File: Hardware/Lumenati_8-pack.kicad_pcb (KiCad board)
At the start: 2 copper layers, 28.4 x 28.4 mm, 38 parts, among them J1 M01PTH, J2 M01PTH, J3 M01PTH, J4 M01PTH, J5 M01PTH, J6 M01PTH, J7 M01PTH, J8 M01PTH, U1 APA102, U2 APA102, U3 APA102, U4 APA102, U5 APA102, U6 APA102, U7 APA102, U8 APA102

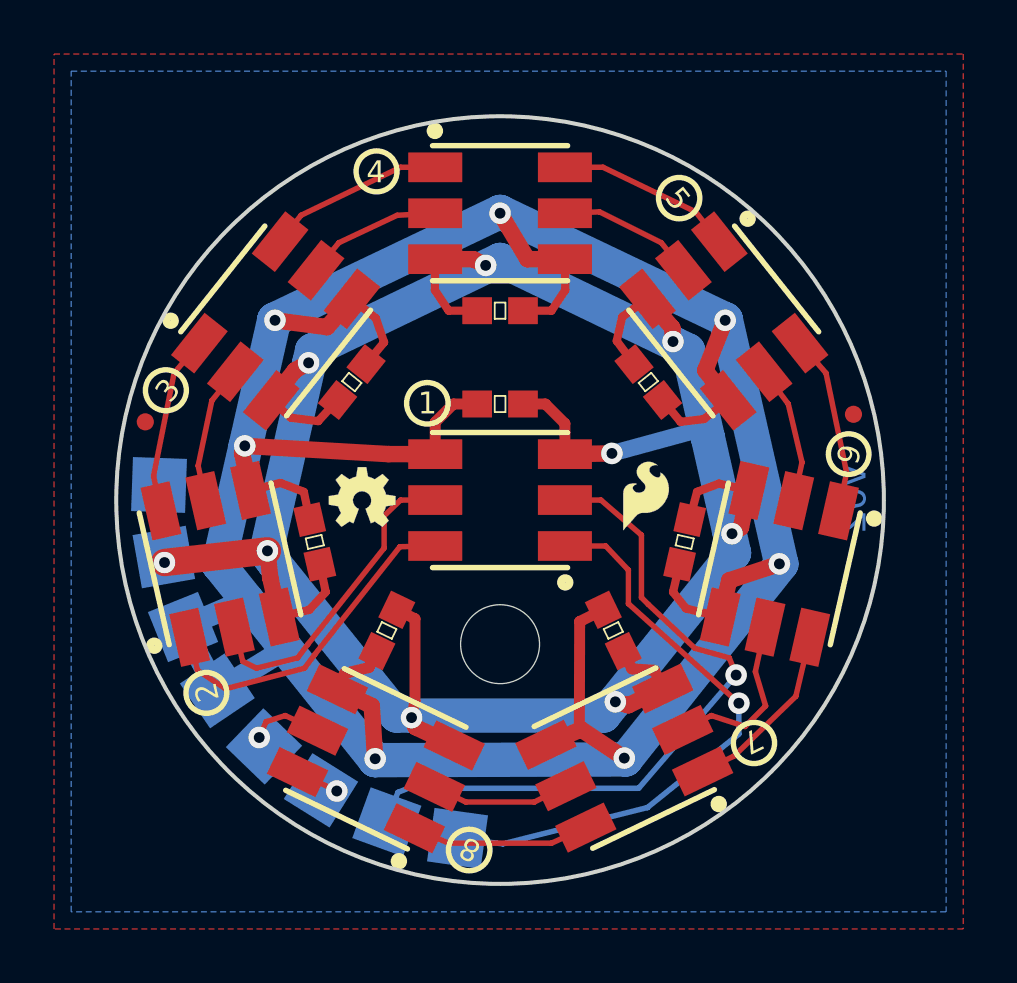
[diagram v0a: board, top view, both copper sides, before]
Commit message: Changed all the names to Lumenati, updated version to v10.
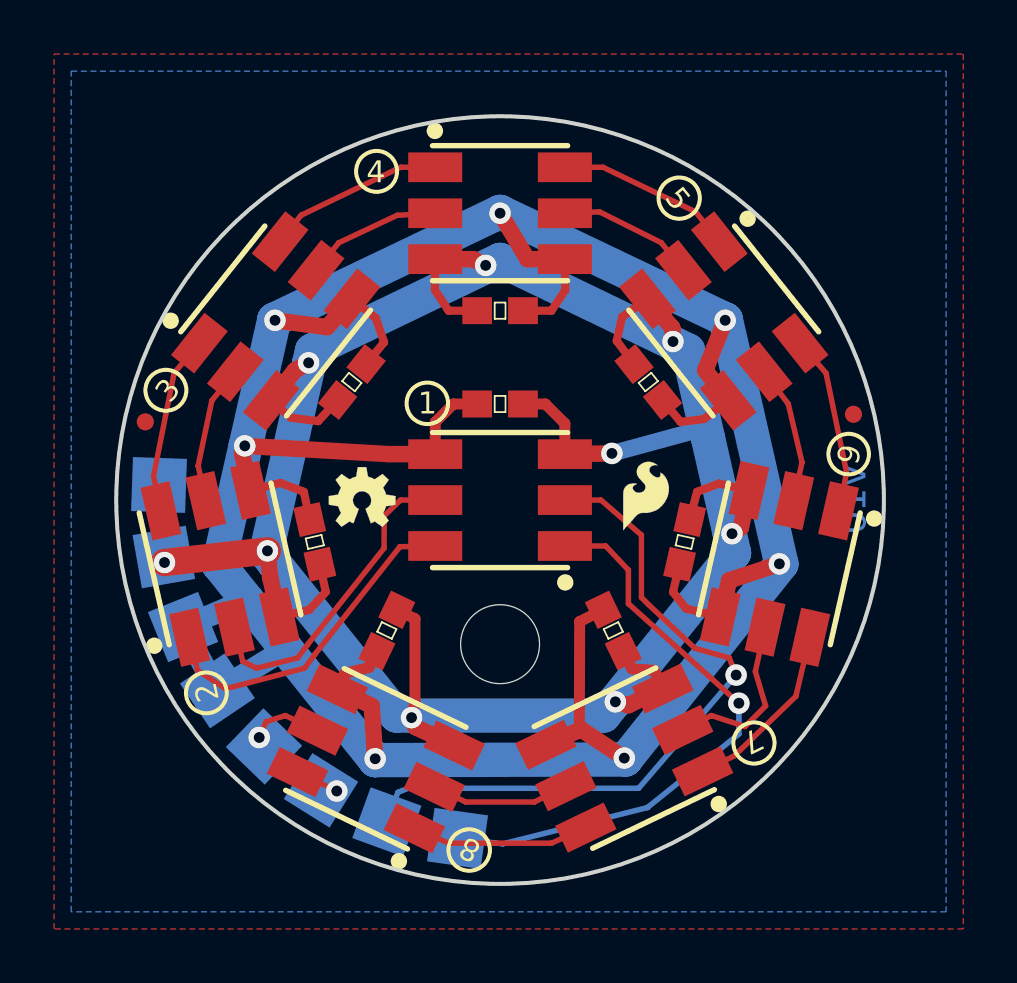
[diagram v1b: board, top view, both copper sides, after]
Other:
- board text added: "Lumenati 8-pack"
- board text added: "v10"
- board text removed: "HiBeam 8-pack"
- board text removed: "HiBeams 8-pack"
- board text removed: "v02"
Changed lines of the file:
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@@
     (35 F.Paste user hide)
     (36 B.SilkS user)
-    (37 F.SilkS user hide)
+    (37 F.SilkS user)
     (38 B.Mask user hide)
     (39 F.Mask user)
-    (40 Dwgs.User user hide)
-    (41 Cmts.User user hide)
+    (40 Dwgs.User user)
+    (41 Cmts.User user)
     (42 Eco1.User user hide)
     (43 Eco2.User user hide)
@@
     (pad_to_mask_clearance 0.1016)
     (aux_axis_origin 0 0)
-    (visible_elements FFF97F7F)
+    (visible_elements FFF9FF7F)
     (pcbplotparams
       (layerselection 0x010fc_ffffffff)
@@
       (net 2 GND))
   )
-  (gr_circle (center 145.542 110.744) (end 146.177 111.1758) (layer F.SilkS) (width 0.2))
-  (gr_circle (center 142.113 85.6234) (end 142.6972 86.106) (layer F.SilkS) (width 0.2))
-  (gr_circle (center 153.3144 86.614) (end 154.0256 86.8934) (layer F.SilkS) (width 0.2))
-  (gr_circle (center 156.083 106.7816) (end 156.7434 107.1626) (layer F.SilkS) (width 0.2))
-  (gr_circle (center 159.5882 96.0882) (end 160.274 96.393) (layer F.SilkS) (width 0.2))
-  (gr_circle (center 135.8138 104.9274) (end 136.3218 105.4862) (layer F.SilkS) (width 0.2))
-  (gr_circle (center 143.9926 94.2086) (end 144.6276 94.6404) (layer F.SilkS) (width 0.2))
-  (gr_circle (center 134.3152 93.726) (end 134.8994 94.2086) (layer F.SilkS) (width 0.2))
+  (gr_circle (center 145.542 110.744) (end 146.177 111.1758) (layer F.SilkS) (width 0.15))
+  (gr_circle (center 142.113 85.6234) (end 142.6972 86.106) (layer F.SilkS) (width 0.15))
+  (gr_circle (center 153.3144 86.614) (end 154.0256 86.8934) (layer F.SilkS) (width 0.15))
+  (gr_circle (center 156.083 106.7816) (end 156.7434 107.1626) (layer F.SilkS) (width 0.15))
+  (gr_circle (center 159.5882 96.0882) (end 160.274 96.393) (layer F.SilkS) (width 0.15))
+  (gr_circle (center 135.8138 104.9274) (end 136.3218 105.4862) (layer F.SilkS) (width 0.15))
+  (gr_circle (center 143.9926 94.2086) (end 144.6276 94.6404) (layer F.SilkS) (width 0.15))
+  (gr_circle (center 134.3152 93.726) (end 134.8994 94.2086) (layer F.SilkS) (width 0.15))
   (gr_text 8 (at 145.5674 110.7186 154.3) (layer F.SilkS)
     (effects (font (size 0.8128 0.8128) (thickness 0.1778)))
@@
     (arrow2b (pts (xy 160.909 128.1938) (xy 159.782496 128.780221)))
   )
-  (gr_text 5/19/17 (at 212.3948 193.0146) (layer Dwgs.User)
+  (gr_text 5/19/17 (at 212.3948 193.0146) (layer Cmts.User)
     (effects (font (size 1.5 1.5) (thickness 0.3)))
   )
-  (gr_text v02 (at 271.2974 193.0654) (layer Dwgs.User)
+  (gr_text v10 (at 271.2974 193.0654) (layer Cmts.User)
     (effects (font (size 1.5 1.5) (thickness 0.3)))
   )
-  (gr_text 1/1 (at 188.468 183.1848) (layer Dwgs.User)
+  (gr_text 1/1 (at 188.468 183.1848) (layer Cmts.User)
     (effects (font (size 1.5 1.5) (thickness 0.3)))
   )
-  (gr_text "HiBeam 8-pack" (at 195.9864 189.6618) (layer Dwgs.User)
+  (gr_text "Lumenati 8-pack" (at 195.9864 189.6618) (layer Cmts.User)
     (effects (font (size 1.5 1.5) (thickness 0.3)))
   )
-  (gr_text "Released under the Creative Commons\nAttribution Share-Alike 4.0 License\nhttps://creativecommons.org/licenses/by-sa/4.0/\nDesigned by Pete Dokter" (at 178.435 173.5074) (layer Dwgs.User)
+  (gr_text "Released under the Creative Commons\nAttribution Share-Alike 4.0 License\nhttps://creativecommons.org/licenses/by-sa/4.0/\nDesigned by Pete Dokter" (at 178.435 173.5074) (layer Cmts.User)
     (effects (font (size 1.5 1.5) (thickness 0.3)) (justify left))
   )
@@
     (effects (font (size 1.016 1.016) (thickness 0.2032)) (justify mirror))
   )
-  (gr_text "HiBeams 8-pack" (at 146.685 92.6592) (layer B.SilkS)
+  (gr_text "Lumenati 8-pack" (at 146.685 92.6592) (layer B.SilkS)
     (effects (font (size 1.5 1.5) (thickness 0.3)) (justify mirror))
   )
-  (gr_text v02 (at 159.7406 97.7646 90) (layer B.Cu)
+  (gr_text v10 (at 159.7406 97.7646 90) (layer B.Cu)
     (effects (font (size 1.016 1.016) (thickness 0.2032)) (justify mirror))
   )
